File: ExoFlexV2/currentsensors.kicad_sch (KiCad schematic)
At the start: 12 parts

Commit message: Many changes
Debouncing, power protection, potentiometer limits, etc.
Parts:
- removed J? (x3): ST5V, symbol Connector:Screw_Terminal_01x02
- removed J? (x6): STCur, symbol Connector:Screw_Terminal_01x02
- removed U? (x3): ACS712, ACS712:SO08, symbol ACS712:ACS712
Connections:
- no-connect marks 15 -> 0
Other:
- note removed: "Current Sensors"

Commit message: quque truc
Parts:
- added TP83, TP84, TP85, TP86, TP87, TP88, TP89, TP90, TP91, TP92: 5005, FootPrint:KEYSTONE_5005, symbol SymLib:5005
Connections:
- new net GND: TP83.TP, TP84.TP, TP85.TP, TP86.TP, TP87.TP, TP88.TP, TP89.TP, TP90.TP, TP91.TP, TP92.TP

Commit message: Placement
Début du placement et modification d'après dernier review
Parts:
- renumbered TP83 to TP121, TP84 to TP122, TP85 to TP123, TP86 to TP124, TP87 to TP125, TP88 to TP126, TP89 to TP127, TP90 to TP128, TP91 to TP129, TP92 to TP130
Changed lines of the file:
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@@
   (symbol (lib_id "SymLib:5005") (at 91.44 17.78 90) (unit 1)
     (in_bom yes) (on_board yes) (fields_autoplaced)
-    (property "Reference" "TP89" (id 0) (at 93.98 16.5099 90)
+    (property "Reference" "TP127" (id 0) (at 93.98 16.5099 90)
       (effects (font (size 1.27 1.27)) (justify right))
     )
@@
   (symbol (lib_id "SymLib:5005") (at 115.57 17.78 90) (unit 1)
     (in_bom yes) (on_board yes) (fields_autoplaced)
-    (property "Reference" "TP91" (id 0) (at 118.11 16.5099 90)
+    (property "Reference" "TP129" (id 0) (at 118.11 16.5099 90)
       (effects (font (size 1.27 1.27)) (justify right))
     )
@@
   (symbol (lib_id "SymLib:5005") (at 19.05 17.78 90) (unit 1)
     (in_bom yes) (on_board yes) (fields_autoplaced)
-    (property "Reference" "TP83" (id 0) (at 21.59 16.5099 90)
+    (property "Reference" "TP121" (id 0) (at 21.59 16.5099 90)
       (effects (font (size 1.27 1.27)) (justify right))
     )
@@
   (symbol (lib_id "SymLib:5005") (at 78.74 17.78 90) (unit 1)
     (in_bom yes) (on_board yes) (fields_autoplaced)
-    (property "Reference" "TP88" (id 0) (at 81.28 16.5099 90)
+    (property "Reference" "TP126" (id 0) (at 81.28 16.5099 90)
       (effects (font (size 1.27 1.27)) (justify right))
     )
@@
   (symbol (lib_id "power:GND") (at 19.05 26.67 0) (unit 1)
     (in_bom yes) (on_board yes) (fields_autoplaced)
-    (property "Reference" "#PWR0229" (id 0) (at 19.05 33.02 0)
+    (property "Reference" "#PWR0210" (id 0) (at 19.05 33.02 0)
       (effects (font (size 1.27 1.27)) hide)
     )
@@
   (symbol (lib_id "SymLib:5005") (at 128.27 17.78 90) (unit 1)
     (in_bom yes) (on_board yes) (fields_autoplaced)
-    (property "Reference" "TP92" (id 0) (at 130.81 16.5099 90)
+    (property "Reference" "TP130" (id 0) (at 130.81 16.5099 90)
       (effects (font (size 1.27 1.27)) (justify right))
     )
@@
   (symbol (lib_id "SymLib:5005") (at 66.04 17.78 90) (unit 1)
     (in_bom yes) (on_board yes) (fields_autoplaced)
-    (property "Reference" "TP87" (id 0) (at 68.58 16.5099 90)
+    (property "Reference" "TP125" (id 0) (at 68.58 16.5099 90)
       (effects (font (size 1.27 1.27)) (justify right))
     )
@@
   (symbol (lib_id "SymLib:5005") (at 43.18 17.78 90) (unit 1)
     (in_bom yes) (on_board yes) (fields_autoplaced)
-    (property "Reference" "TP85" (id 0) (at 45.72 16.5099 90)
+    (property "Reference" "TP123" (id 0) (at 45.72 16.5099 90)
       (effects (font (size 1.27 1.27)) (justify right))
     )
@@
   (symbol (lib_id "SymLib:5005") (at 102.87 17.78 90) (unit 1)
     (in_bom yes) (on_board yes) (fields_autoplaced)
-    (property "Reference" "TP90" (id 0) (at 105.41 16.5099 90)
+    (property "Reference" "TP128" (id 0) (at 105.41 16.5099 90)
       (effects (font (size 1.27 1.27)) (justify right))
     )
@@
   (symbol (lib_id "SymLib:5005") (at 54.61 17.78 90) (unit 1)
     (in_bom yes) (on_board yes) (fields_autoplaced)
-    (property "Reference" "TP86" (id 0) (at 57.15 16.5099 90)
+    (property "Reference" "TP124" (id 0) (at 57.15 16.5099 90)
       (effects (font (size 1.27 1.27)) (justify right))
     )
@@
   (symbol (lib_id "SymLib:5005") (at 30.48 17.78 90) (unit 1)
     (in_bom yes) (on_board yes) (fields_autoplaced)
-    (property "Reference" "TP84" (id 0) (at 33.02 16.5099 90)
-      (effects (font (size 1.27 1.27)) (justify right))
-    )
+    (property "Reference" "TP122" (id 0) (at 33.02 16.5099 90)
+      (effects (font (size 1.27 1.27)) (justify right))
+    )

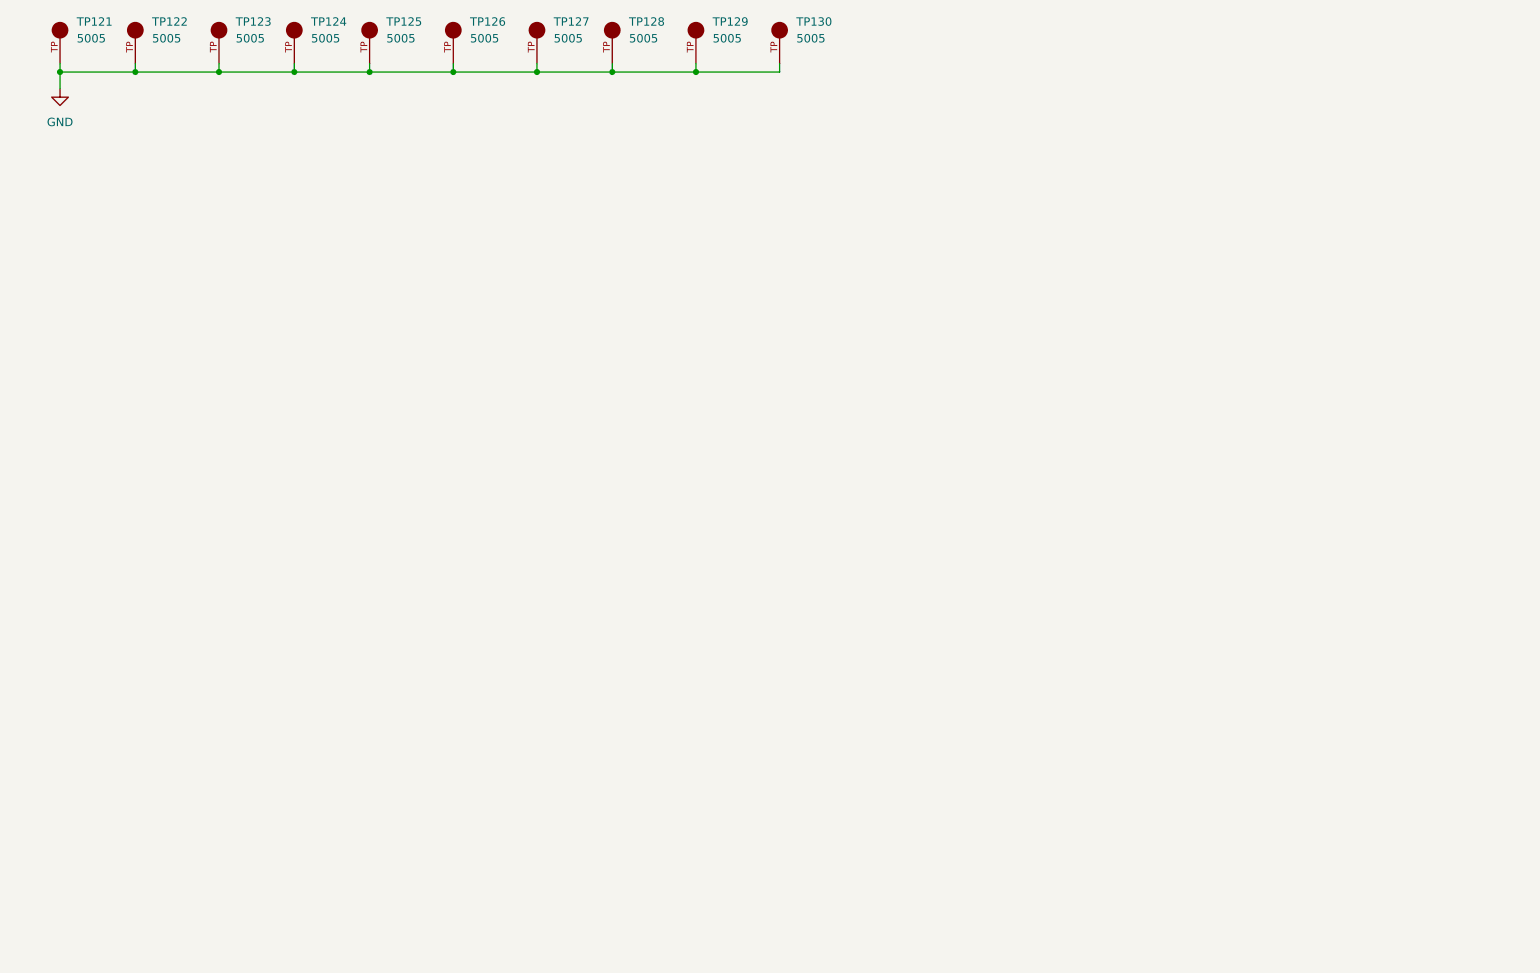
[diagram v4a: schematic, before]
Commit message: Mise à jour mi-stage
- Torque et Amplitude testé et vérifié
- Capteur de présence et de proximité testé
- Système de détection de coupure de fils
- Polyvalence pour plusieurs capteurs
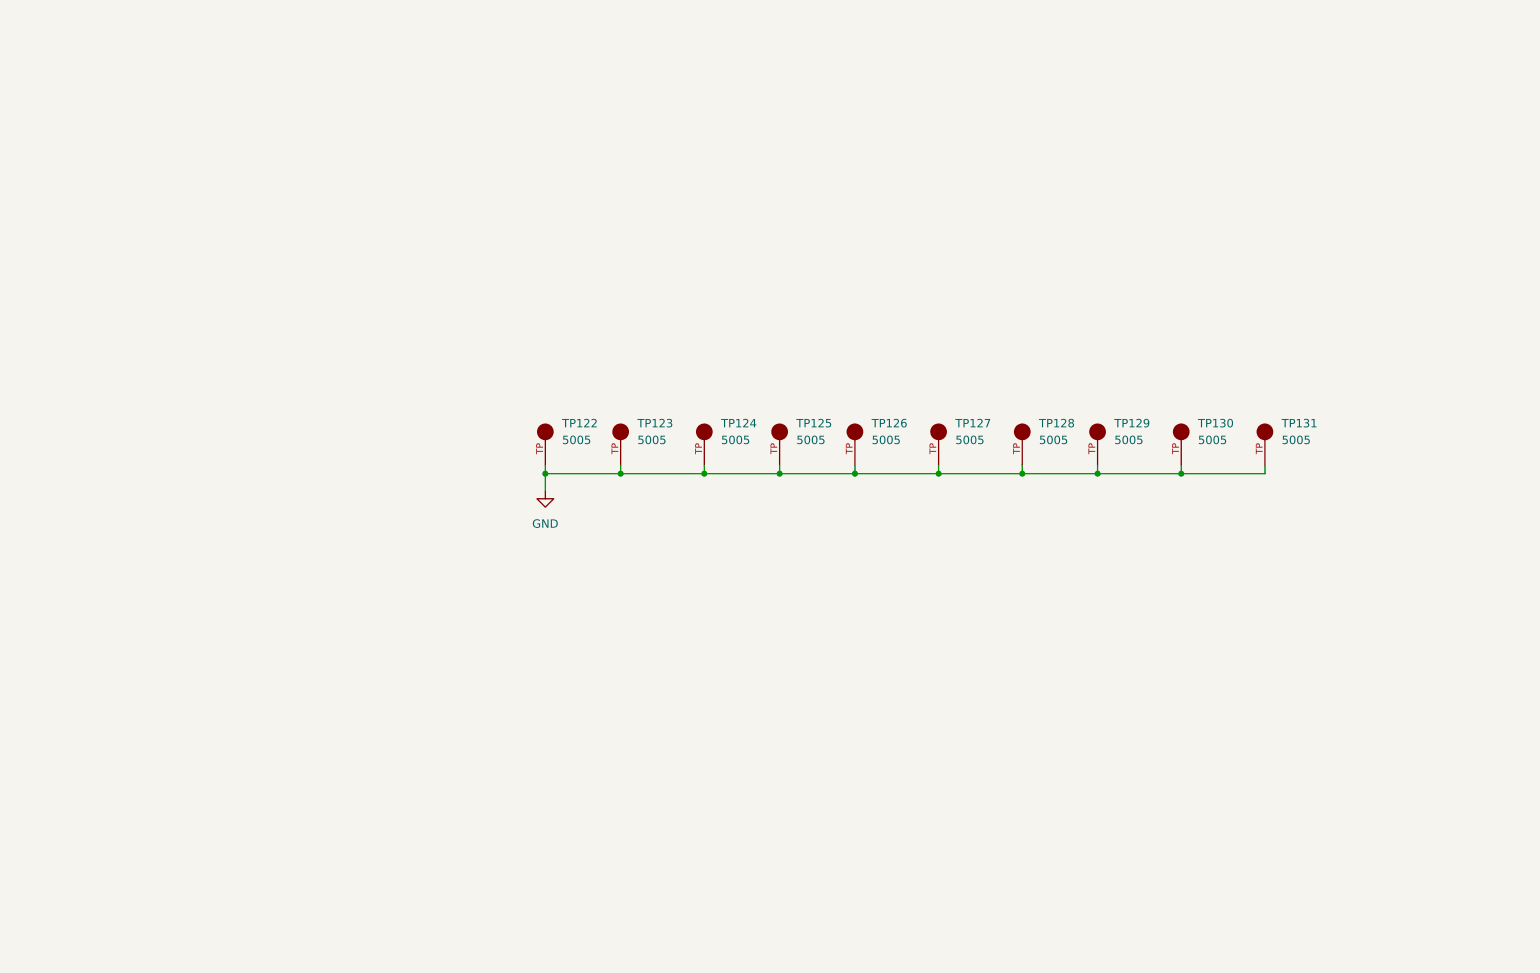
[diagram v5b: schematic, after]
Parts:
- renumbered TP121 to TP122, TP122 to TP123, TP123 to TP124, TP124 to TP125, TP125 to TP126, TP126 to TP127, TP127 to TP128, TP128 to TP129, TP129 to TP130, TP130 to TP131
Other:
- moved on the sheet: TP122, TP123, TP124, TP125, TP126, TP127, TP128, TP129, TP130, TP131

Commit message: Mise à jour signaux STM
- Condo de découplage
- Signaux supplémentaire pour le STM
- Page GND sera pour Multiplexeur
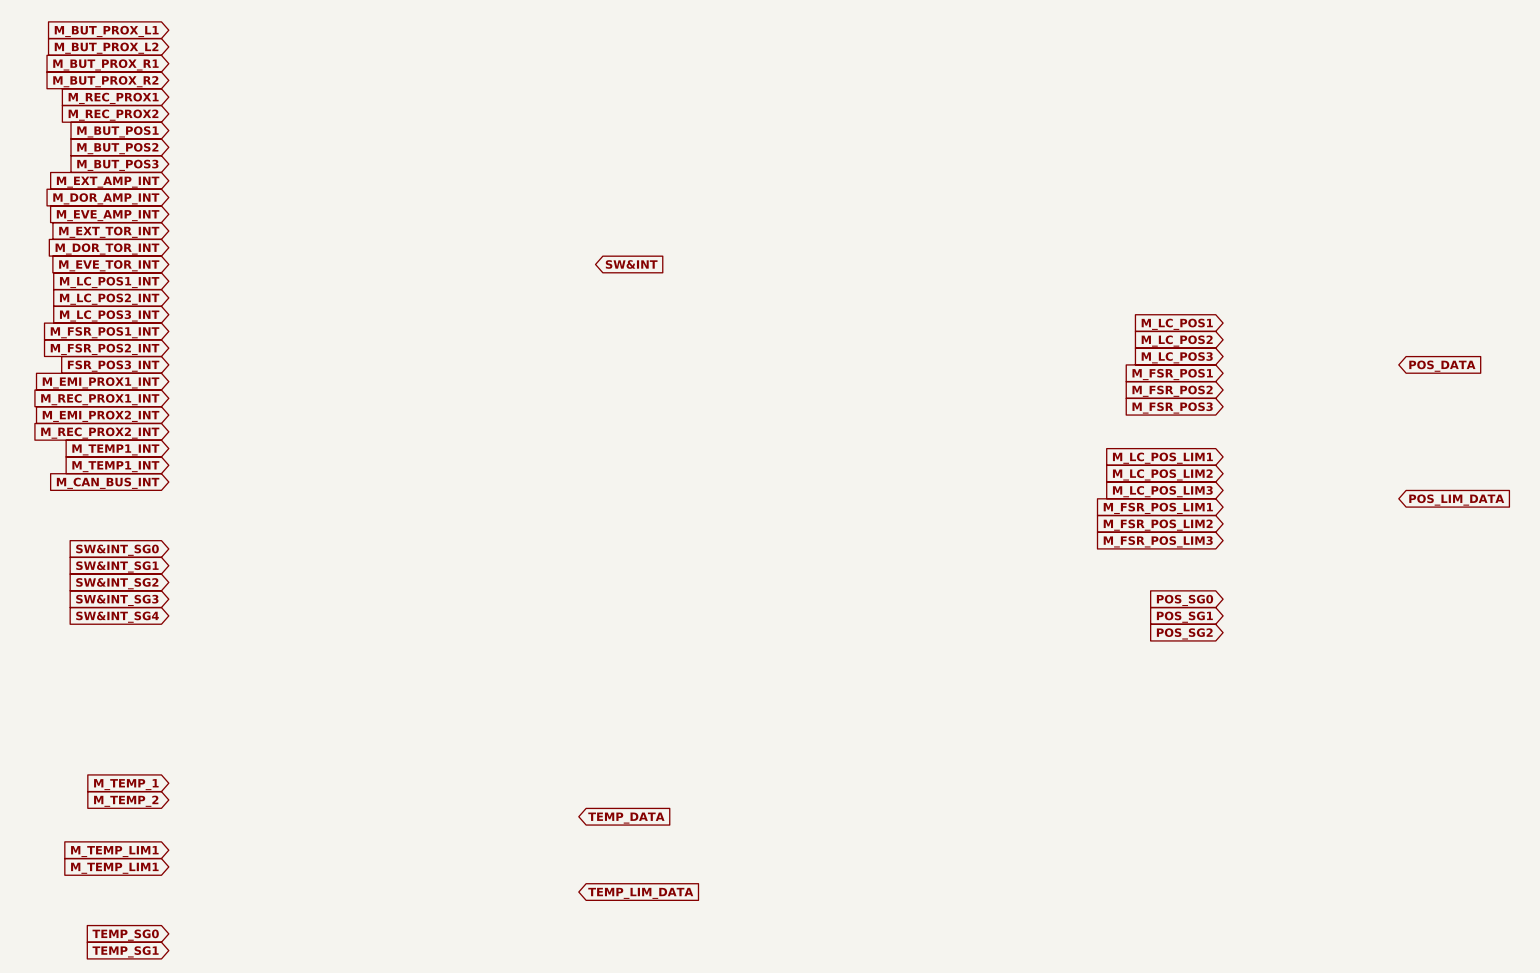
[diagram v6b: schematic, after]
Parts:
- removed TP122, TP123, TP124, TP125, TP126, TP127, TP128, TP129, TP130, TP131: 5005, FootPrint:KEYSTONE_5005, symbol SymLib:5005
